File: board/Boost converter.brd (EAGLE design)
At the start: 25.1 x 63.5 mm, 21 parts, among them IC1 NE555N, IC2 attiny84, IC3 attiny85, Q1 2n7000, Q2 zvp4105

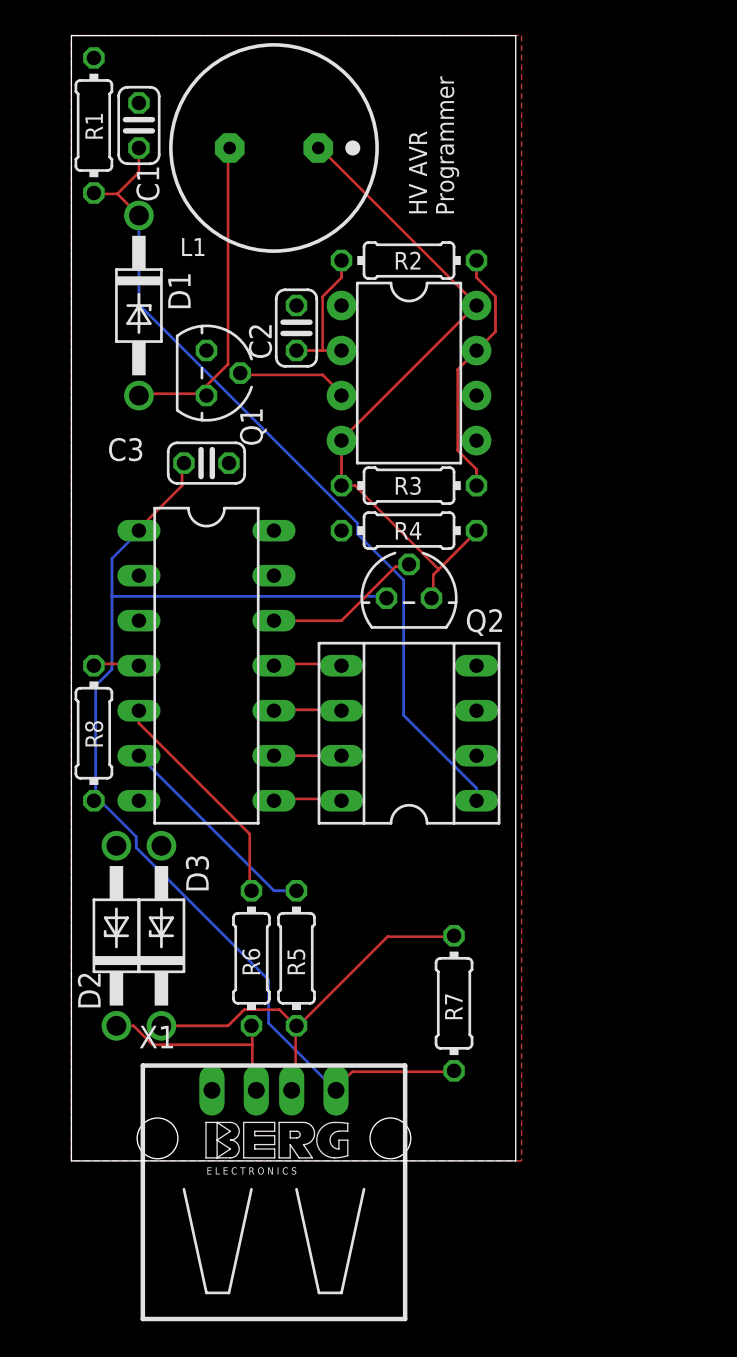
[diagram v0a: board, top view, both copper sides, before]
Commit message: added v-usb library and done routing board
added v-usb library, but still need to change settings in usbconfig.h. also usb needs to use only one port for both d+ and d- lines (d+ can't be on pa0 and d- on pb1) so I had to change the usb data lines again. d+ is on PA0 with pcint0 and d- is on PA7. attiny85 pin 2 is now on PA6
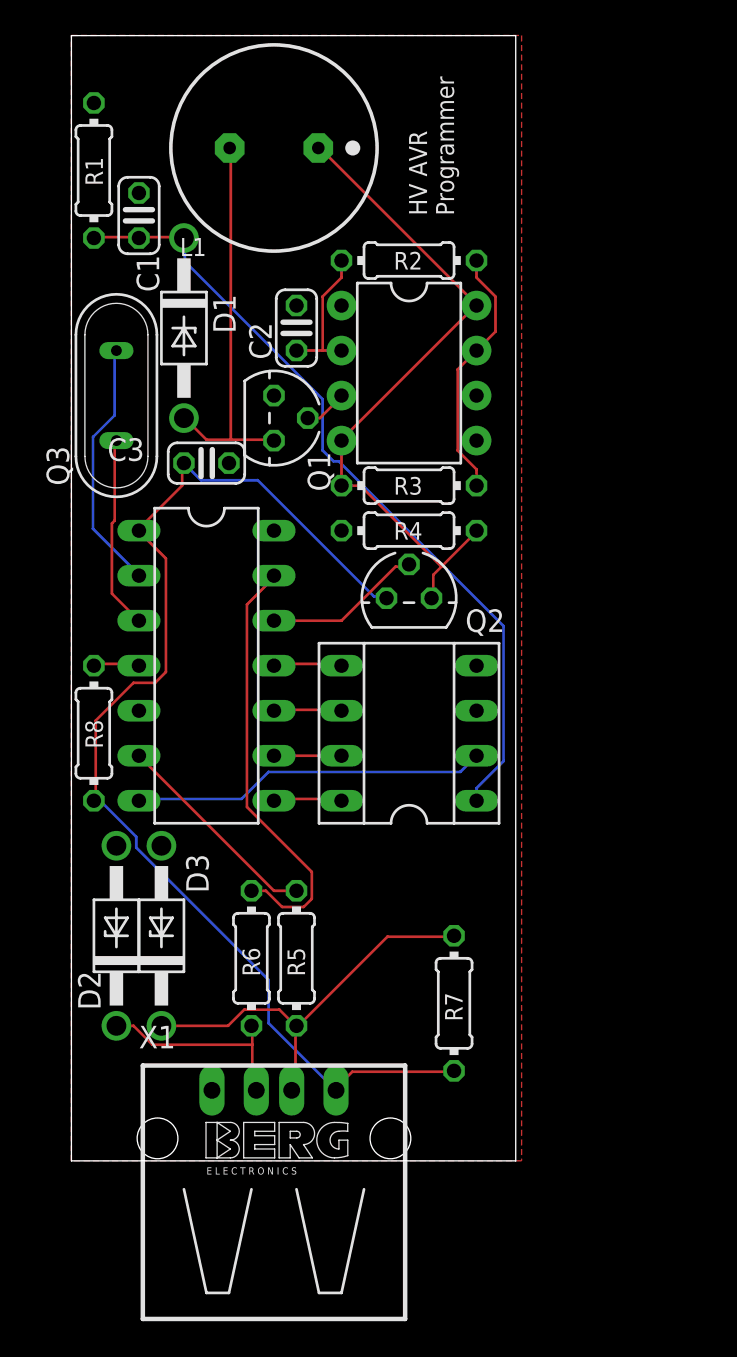
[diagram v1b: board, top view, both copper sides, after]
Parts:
- added Q3: (no value), special:QS
- moved C1 5.08 mm to (3.81, 53.3)
- moved Q1 4.58 mm to (11.4, 41.9)
- moved D1 2.84 mm to (6.35, 47.0)
- moved R1 2.54 mm to (1.27, 55.9)
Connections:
- new net N$17: IC2.7, IC3.2
- new net N$4: IC2.13, R6.2
- net N$11: now also IC2.2, Q3.2; no longer IC2.13, IC3.2
- net N$5: now also IC2.3, Q3.1; no longer IC2.5, R6.2
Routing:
- net N$4: track 0.00 -> 24.4 mm
- net N$17: track 0.00 -> 20.2 mm
- net N$11: track 0.00 -> 14.4 mm
- net N$14: track 6.31 -> 2.46 mm
- net N$15: track 18.5 -> 22.2 mm
- net N$5: track 12.8 -> 10.9 mm
- net V+: track 47.1 -> 45.2 mm
- net VCC: track 66.4 -> 67.1 mm

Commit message: Added crystal oscillator and potentiometer to board
crystal oscillator is next to ATtiny84 and potentiometer is next to inductor and 555. also moved around boost converter components so they are located in the same places as in the first version of the board. I should double check potentiometer sizes before having this board manufactured. Also should probably double check calculations and test current board with same signal diode and potentiometer to see actual range vs calculated range of output voltage
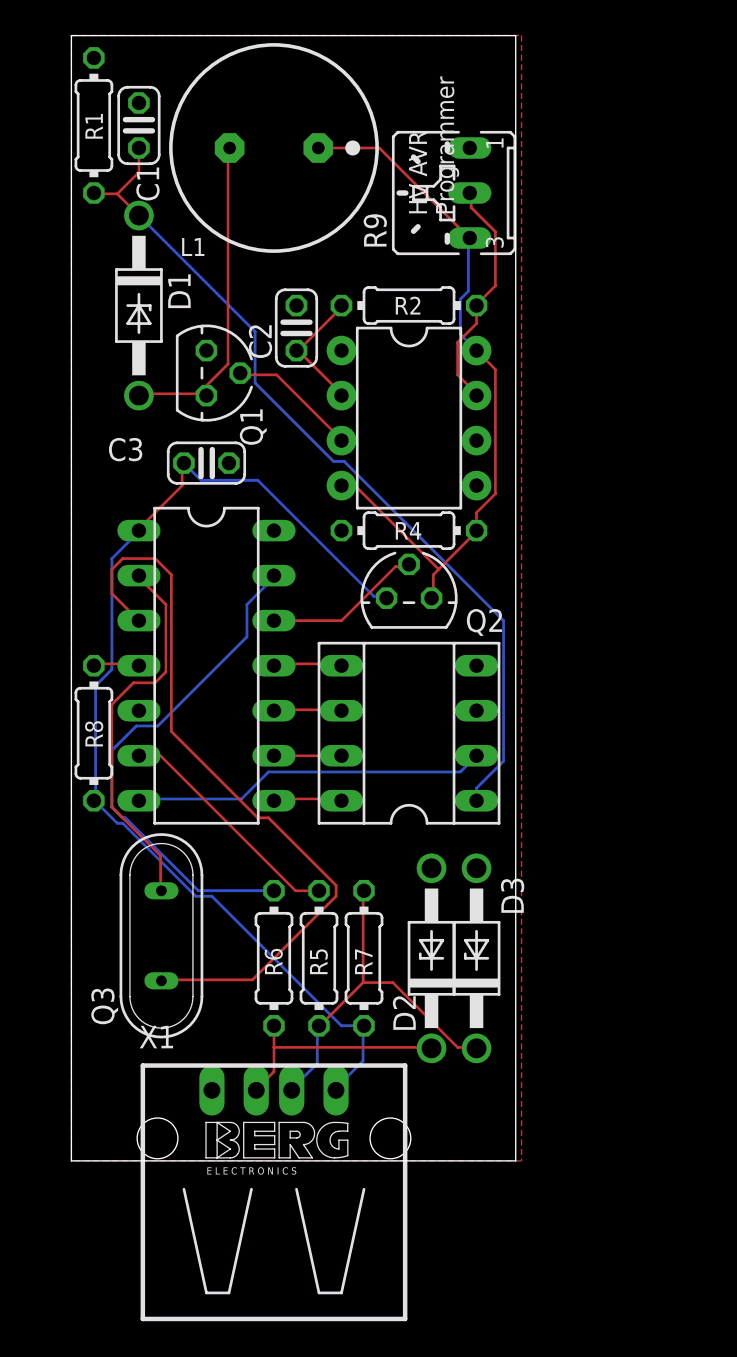
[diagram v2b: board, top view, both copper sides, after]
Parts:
- removed R3: (no value), resistor:0204/7
- added R9: (no value), pot:B25U
- moved Q3 30.6 mm to (5.08, 12.7)
- moved D2 17.8 mm to (20.3, 11.4)
- moved D3 17.8 mm to (22.9, 11.4)
- moved R7 5.68 mm to (16.5, 11.4)
- moved C1 5.08 mm to (3.81, 58.4)
- moved Q1 4.58 mm to (7.62, 44.5)
- moved D1 2.84 mm to (3.81, 48.3)
- moved IC1 2.54 mm to (19.1, 41.9)
- moved R1 2.54 mm to (1.27, 58.4)
- moved R2 2.54 mm to (19.1, 48.3)
- moved R5 1.27 mm to (14.0, 11.4)
- moved R6 1.27 mm to (11.4, 11.4)
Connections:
- removed net N$12: IC1.7, R2.1, R3.1
- new net N$18: IC1.7, R2.1, R9.S
- net +5V: now also R9.E; no longer R3.2
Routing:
- net N$5: track 10.9 -> 41.7 mm
- net N$12: track 14.5 -> 0.00 mm
- net N$18: track 0.00 -> 13.4 mm
- net N$11: track 14.4 -> 21.6 mm
- net VCC: track 67.1 -> 60.5 mm
- net N$14: track 2.46 -> 7.33 mm
- net N$4: track 24.4 -> 28.7 mm
- net N$15: track 22.2 -> 18.5 mm
- net V+: track 45.2 -> 48.7 mm
- net +5V: track 38.4 -> 40.9 mm
- net N$3: track 23.1 -> 21.0 mm
- net N$16: track 12.0 -> 13.3 mm
- net N$2: track 11.9 -> 13.0 mm
- net N$13: track 8.06 -> 7.20 mm

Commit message: Board Version 2
Updated board to include crystal oscillator and caps, boost converter feedback loop with resistor divider and mosfet inverter to trigger 555 reset pin and cmos for supplying 12V to t85 reset pin. Dimensions also changed to 1.4" by 2" to accomodate the new components
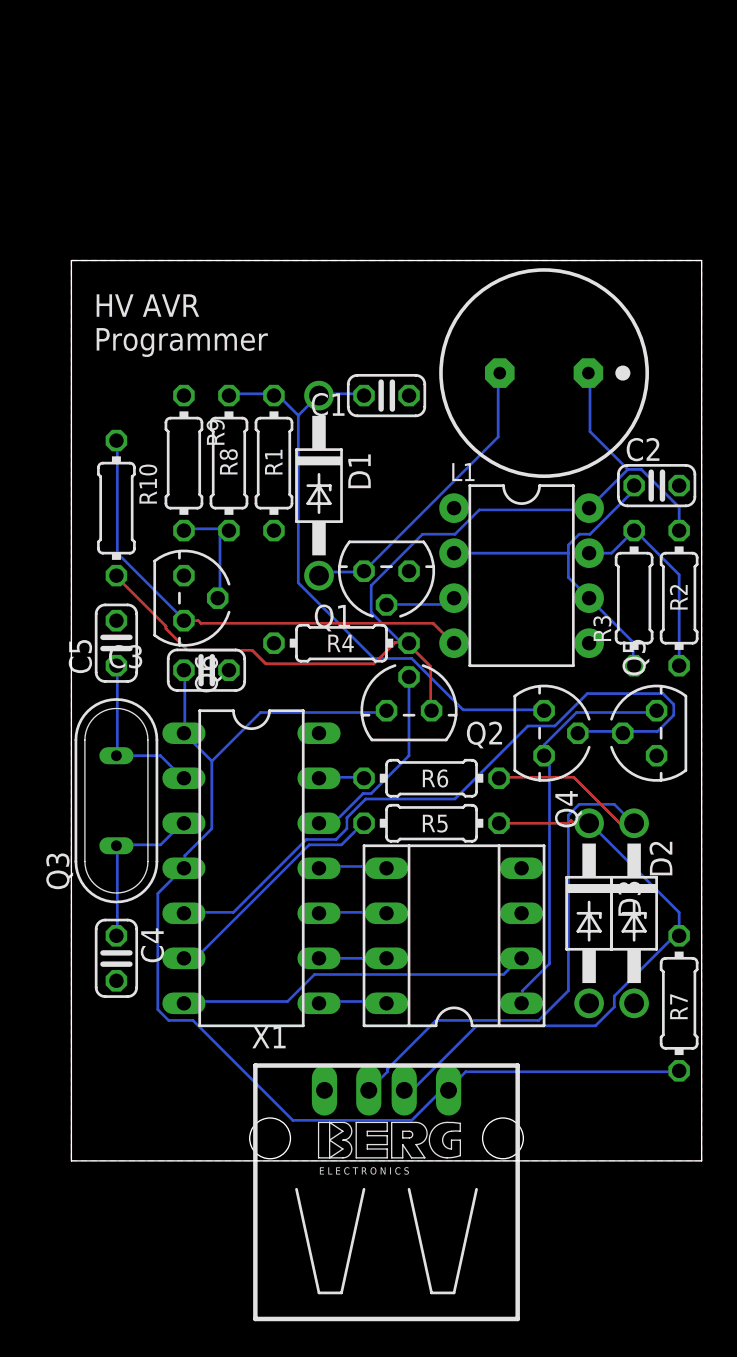
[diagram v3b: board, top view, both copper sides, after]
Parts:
- added C4, C5: 36pF, resistor:C025-024X044
- added Q4: zvp4105, transistor2:TO-92
- added Q5: zvn3306a, transistor2:TO-92
- added Q6: 2n7000, transistor2:TO-92
- added R10: 1k, resistor:0204/7
- added R3: 910, resistor:0204/7
- D1: value 1N4728 -> 1N914B
- R1: value 2.2k -> 10k
- R2: value (none) -> 650
- R8: value 10k -> 100k
- R9: value (none) -> 15k; device pot:B25U -> resistor:0204/7
- moved R2 22.5 mm to (34.3, 31.8), turned to 90 degrees
- moved C2 22.2 mm to (33.0, 38.1), turned to 0 degrees
- moved R1 21.6 mm to (11.4, 39.4), turned to 90 degrees
- moved R9 21.6 mm to (6.35, 39.4), turned to 270 degrees
- moved C1 20.7 mm to (17.8, 43.2), turned to 0 degrees
- moved L1 19.8 mm to (26.7, 44.5)
- moved R7 18.0 mm to (34.3, 8.89)
- moved R8 17.0 mm to (8.89, 39.4), turned to 90 degrees
- moved Q1 15.1 mm to (17.8, 33.3), turned to 180 degrees
- moved D1 14.4 mm to (14.0, 38.1)
- moved R6 13.5 mm to (20.3, 21.6), turned to 180 degrees
- moved D2 11.7 mm to (31.8, 14.0), turned to 270 degrees
- moved IC2 11.7 mm to (10.2, 16.5)
- moved IC3 11.7 mm to (21.6, 12.7)
- moved C3 11.7 mm to (7.62, 27.7)
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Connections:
- removed net +5V: IC1.4, IC1.8, L1.1, Q2.3, R4.1, R9.E
- removed net N$1 (its old number): IC2.4, R8.1
- removed net N$18: IC1.7, R2.1, R9.S
- removed net N$5 (its old number): IC2.3, Q3.1
- removed net V+: C1.1, D1.C, IC3.1, R1.2
- new net N$14: C2.1, IC1.2, IC1.6, R3.1
- new net N$16: IC3.1, Q4.3, Q5.3
- new net N$17: IC2.5, Q4.2, Q5.2
- new net N$2: C5.1, IC2.2, Q3.2
- new net N$3: C4.1, IC2.3, Q3.1
- new net N$7: IC1.8, L1.1, Q2.3, R10.2, R2.2, R4.1
- new net N$8: Q6.2, R8.1, R9.2
- new net N$9: IC1.4, Q6.3, R10.1
- net GND: now also C4.2, C5.2, Q5.1, Q6.1, R9.1
- net N$11: now also C1.1, D1.C, Q4.1, R1.2, R8.2; no longer IC2.2, Q3.2
- net N$13: now also IC1.7, R2.1, R3.2; no longer C2.1, IC1.2, R2.2
- net VCC: now also IC2.4; no longer R8.2
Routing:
- net N$7: track 0.00 -> 56.6 mm
- net V+: track 48.7 -> 0.00 mm
- net N$5 (its old number): track 41.7 -> 0.00 mm
- net +5V: track 40.9 -> 0.00 mm
- net N$17: track 0.00 -> 39.9 mm
- net N$9: track 0.00 -> 27.6 mm
- net N$6: track 28.7 -> 2.58 mm
- net N$1: track 13.0 -> 36.7 mm
- net N$16: track 0.00 -> 22.5 mm
- net N$14: track 0.00 -> 20.1 mm
- net N$11: track 21.6 -> 35.2 mm
- net N$18: track 13.4 -> 0.00 mm
- net N$4: track 21.0 -> 33.4 mm
- net N$3: track 0.00 -> 9.44 mm
- net N$2: track 0.00 -> 9.43 mm
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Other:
- board size 25.1 x 63.5 mm -> 35.6 x 50.8 mm
